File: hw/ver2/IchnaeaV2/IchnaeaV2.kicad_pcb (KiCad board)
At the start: 4 copper layers, 100 x 100 mm, 187 parts, among them J1 Screw_Terminal_01x09, J2 Screw_Terminal_01x09, J3 Screw_Terminal_01x09, Q1 BSS138, Q10 MCAC80N10Y, Q11 MCAC80N10Y, Q12 MCAC80N10Y, Q13 MCAC80N10Y, Q14 MCAC80N10Y, Q15 MCAC80N10Y, Q16 MCAC80N10Y, Q17 MCAC80N10Y, Q18 MCAC80N10Y, Q19 MCAC80N10Y, Q2 MCAC80N10Y, Q20 MCAC80N10Y, Q21 MCAC80N10Y, Q22 MCAC80N10Y, Q23 MCAC80N10Y, Q24 MCAC80N10Y, Q25 MCAC80N10Y, Q26 BSS138, Q27 BSS84, Q28 BSS138, Q29 BSS138, Q3 MCAC80N10Y, Q4 MCAC80N10Y, Q5 MCAC80N10Y, Q6 MCAC80N10Y, Q7 MCAC80N10Y, Q8 MCAC80N10Y, Q9 MCAC80N10Y, U1 LTC7871, U2 HIP2210, U3 HIP2210, U4 HIP2210, U5 HIP2210, U6 HIP2210, U7 HIP2210

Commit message: Sync work to main PC
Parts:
- removed D2, D3, D4, D5, D6, D7: Z5V1, Diode_SMD:D_SOD-123
- removed JP1, JP2: SolderJumper_2_Bridged, Jumper:SolderJumper-2_P1.3mm_Bridged_Pad1.0x1.5mm
- added C74: 10uF, Capacitor_SMD:C_0603_1608Metric, F.Cu at (162.4, 39.7)
- added C75: 4.7uF, Capacitor_SMD:C_0603_1608Metric, F.Cu at (162.4, 42.2)
- added C76: 100nF, Capacitor_SMD:C_0603_1608Metric, F.Cu at (162.4, 44.7)
- added C77: 47pF, Capacitor_SMD:C_0603_1608Metric, F.Cu at (162.4, 47.2)
- added C78: 10uF, Capacitor_SMD:C_0603_1608Metric, F.Cu at (166.4, 39.7)
- added C79: 10uF, Capacitor_SMD:C_0603_1608Metric, F.Cu at (166.4, 42.2)
- added C80: 10uF, Capacitor_SMD:C_0603_1608Metric, F.Cu at (166.4, 44.7)
- added C81: 10uF, Capacitor_SMD:C_0603_1608Metric, F.Cu at (166.4, 47.2)
- added C82: 10uF-100v, Capacitor_SMD:C_1210_3225Metric_Pad1.33x2.70mm_HandSolder, B.Cu at (168.1, 102.7)
- added C83: 10uF-100v, Capacitor_SMD:C_1210_3225Metric_Pad1.33x2.70mm_HandSolder, B.Cu at (171.4, 102.7)
- added D10: PMEG10010ELRX, Diode_SMD:D_SOD-123, F.Cu at (175.3, 40.1)
- added L7: 22uH, Inductors:TYS5020220M, F.Cu at (169.7, 51.5)
- added R54: 0, Resistor_SMD:R_0603_1608Metric, F.Cu at (126.7, 120.0)
- added R56: 0, Resistor_SMD:R_0603_1608Metric, F.Cu at (126.7, 121.2)
- added R57: 68k, Resistor_SMD:R_0603_1608Metric, F.Cu at (170.4, 39.7)
- added R58: 510k, Resistor_SMD:R_0603_1608Metric, F.Cu at (170.4, 42.2)
- added R59: 7.5k, Resistor_SMD:R_0603_1608Metric, F.Cu at (170.4, 44.7)
- added R60: 100k, Resistor_SMD:R_0603_1608Metric, F.Cu at (170.4, 47.2)
- added R61: 10k, Resistor_SMD:R_0603_1608Metric, F.Cu at (123.7, 117.6)
- added R62: 0, Resistor_SMD:R_0603_1608Metric, F.Cu at (126.7, 91.5)
- added R63: 0, Resistor_SMD:R_0603_1608Metric, F.Cu at (126.7, 90.0)
- added R64: 10k, Resistor_SMD:R_0603_1608Metric, F.Cu at (123.7, 87.9)
- added R65: 6.2k, Resistor_SMD:R_0603_1608Metric, F.Cu at (126.1, 87.2)
- added R66: 10k, Resistor_SMD:R_0603_1608Metric, F.Cu at (132.8, 84.2)
- added R67: 6.2k, Resistor_SMD:R_0603_1608Metric, F.Cu at (132.8, 87.2)
- added R68: 0, Resistor_SMD:R_0603_1608Metric, F.Cu at (160.1, 87.2)
- added R69: 10k, Resistor_SMD:R_0603_1608Metric, F.Cu at (162.3, 84.2)
- added R70: 6.2k, Resistor_SMD:R_0603_1608Metric, F.Cu at (163.8, 84.2)
- added R71: 0, Resistor_SMD:R_0603_1608Metric, F.Cu at (163.2, 90.9)
- added R72: 10k, Resistor_SMD:R_0603_1608Metric, F.Cu at (166.2, 93.1)
- added R73: 6.2k, Resistor_SMD:R_0603_1608Metric, F.Cu at (163.2, 93.1)
- added R74: 0, Resistor_SMD:R_0603_1608Metric, F.Cu at (163.3, 120.1)
- added R75: 10k, Resistor_SMD:R_0603_1608Metric, F.Cu at (166.3, 122.4)
- added R76: 6.2k, Resistor_SMD:R_0603_1608Metric, F.Cu at (163.3, 122.4)
- added U8: AP66200FVBW-13, Package_DFN_QFN:QFN-16-1EP_4x4mm_P0.65mm_EP2.5x2.5mm, F.Cu at (163.5, 51.6)
- C13, C19, C25, C31: value 100nF -> 10uF-100v; footprint Capacitor_SMD:C_0603_1608Metric -> Capacitor_SMD:C_1210_3225Metric_Pad1.33x2.70mm_HandSolder; moved to B.Cu
- D1: value SS210 -> SB10100L; footprint Diode_SMD:D_SMA -> Package_TO_SOT_SMD:TO-277A
- R12, R16, R20, R4, R8: value 2k -> 0
- R24: value 2k -> 6.2k
- moved J3 85.9 mm to (140.6, 144.0)
- moved C1 69.8 mm to (76.1, 134.1)
- moved C2 69.8 mm to (76.1, 136.6)
- moved R1 69.8 mm to (76.1, 144.1)
- moved R2 69.8 mm to (76.1, 146.6)
- moved R3 69.8 mm to (76.1, 149.1)
- moved R46 69.8 mm to (70.9, 143.0)
- moved R49 69.8 mm to (67.2, 145.2)
- moved R50 69.8 mm to (67.2, 147.7)
- moved C5 69.8 mm to (77.1, 156.0)
- moved D1 69.8 mm to (70.1, 156.1)
- moved Q1 69.8 mm to (82.6, 156.2)
- moved Q28 69.8 mm to (69.8, 139.7)
- moved Q29 69.8 mm to (72.0, 147.6)
- moved R51 69.8 mm to (69.5, 147.7)
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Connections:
- C12 pad 1: +VSW -> +12V
- C13 pad 1: +VSW -> VHIGH
- C18 pad 1: +VSW -> +12V
- C19 pad 1: +VSW -> VHIGH
- C24 pad 1: +VSW -> +12V
- C25 pad 1: +VSW -> VHIGH
- C30 pad 1: +VSW -> +12V
- C31 pad 1: +VSW -> VHIGH
- C36 pad 1: +VSW -> +12V
- C6 pad 1: +VSW -> +12V
- D1 pad 1: Net-(D1-K) -> VLOW
- L1 pad 1: Net-(Q2-S) -> VLOW
- L1 pad 2: VLOW -> Net-(Q2-S)
- L2 pad 1: VLOW -> Net-(Q6-S)
- L2 pad 2: Net-(Q6-S) -> VLOW
- L3 pad 1: Net-(Q10-S) -> VLOW
- L3 pad 2: VLOW -> Net-(Q10-S)
- L4 pad 1: VLOW -> Net-(Q14-S)
- L4 pad 2: Net-(Q14-S) -> VLOW
- L5 pad 1: Net-(Q18-S) -> VLOW
- L5 pad 2: VLOW -> Net-(Q18-S)
- L6 pad 1: VLOW -> Net-(Q22-S)
- L6 pad 2: Net-(Q22-S) -> VLOW
- R12 pad 1: Net-(D4-K) -> Net-(U4-EN)
- R12 pad 2: +VSW -> /PowerStage/Phase1/PWMEN
- R16 pad 1: Net-(D5-K) -> Net-(U5-EN)
- R16 pad 2: +VSW -> /PowerStage/Phase1/PWMEN
- R20 pad 1: Net-(D6-K) -> Net-(U5-PWM)
- R20 pad 2: +VSW -> /PowerStage/Phase4/PWM
- R24 pad 2: +VSW -> GND
- R4 pad 1: Net-(D2-K) -> Net-(U2-EN)
- R4 pad 2: +VSW -> /PowerStage/Phase1/PWMEN
- R8 pad 1: Net-(D3-K) -> Net-(U3-EN)
- R8 pad 2: +VSW -> /PowerStage/Phase1/PWMEN
- U2 pad 1: +VSW -> +12V
- U2 pad 5: Net-(D2-K) -> Net-(U2-VREF)
- U2 pad 7: /PowerStage/Phase1/PWMEN -> Net-(U2-EN)
- U3 pad 1: +VSW -> +12V
- U3 pad 5: Net-(D3-K) -> Net-(U3-VREF)
- U3 pad 7: /PowerStage/Phase1/PWMEN -> Net-(U3-EN)
- U3 pad 8: /PowerStage/Phase2/PWM -> Net-(U3-PWM)
- U4 pad 1: +VSW -> +12V
- U4 pad 5: Net-(D4-K) -> Net-(U4-VREF)
- U4 pad 7: /PowerStage/Phase1/PWMEN -> Net-(U4-EN)
- U4 pad 8: /PowerStage/Phase3/PWM -> Net-(U4-PWM)
- U5 pad 1: +VSW -> +12V
- U5 pad 5: Net-(D5-K) -> Net-(U5-VREF)
- U5 pad 7: /PowerStage/Phase1/PWMEN -> Net-(U5-EN)
- U5 pad 8: /PowerStage/Phase4/PWM -> Net-(U5-PWM)
- U6 pad 1: +VSW -> +12V
- U6 pad 5: Net-(D6-K) -> Net-(U6-VREF)
- U6 pad 7: /PowerStage/Phase1/PWMEN -> Net-(U6-EN)
- U6 pad 8: /PowerStage/Phase5/PWM -> Net-(U6-PWM)
- U7 pad 1: +VSW -> +12V
- U7 pad 7: /PowerStage/Phase1/PWMEN -> Net-(U7-EN)
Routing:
- net +12V: track 0.00 -> 54.6 mm, vias 0 -> 14
- net GND: track 2.74 -> 43.4 mm, vias 18 -> 49
- net Net-(Q14-G): track 0.00 -> 18.1 mm
- net Net-(Q22-G): track 0.00 -> 18.0 mm
- net Net-(Q6-G): track 0.00 -> 17.9 mm
- net Net-(Q23-G): track 0.00 -> 17.2 mm
- net Net-(Q15-G): track 0.00 -> 17.0 mm
- net Net-(Q7-G): track 0.00 -> 16.9 mm
- net Net-(Q3-G): track 0.00 -> 15.1 mm
- net Net-(Q11-G): track 0.00 -> 14.9 mm
- net Net-(U3-VREF): track 0.00 -> 14.8 mm
- net Net-(Q19-G): track 0.00 -> 14.8 mm
- net Net-(U5-VREF): track 0.00 -> 14.6 mm
- net Net-(U7-VREF): track 0.00 -> 14.1 mm
- net Net-(Q2-G): track 0.00 -> 13.5 mm
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- added copper zone on In2.Cu, net +12V
- added copper zone on F.Cu, net Net-(Q10-S)
- added copper zone on F.Cu, net Net-(Q14-S)
- added copper zone on F.Cu, net Net-(Q18-S)
- added copper zone on F.Cu, net Net-(Q2-S)
- added copper zone on F.Cu, net Net-(Q6-S)
- removed copper zone on F.Cu, net VHIGH
- removed copper zone on B.Cu, net VLOW

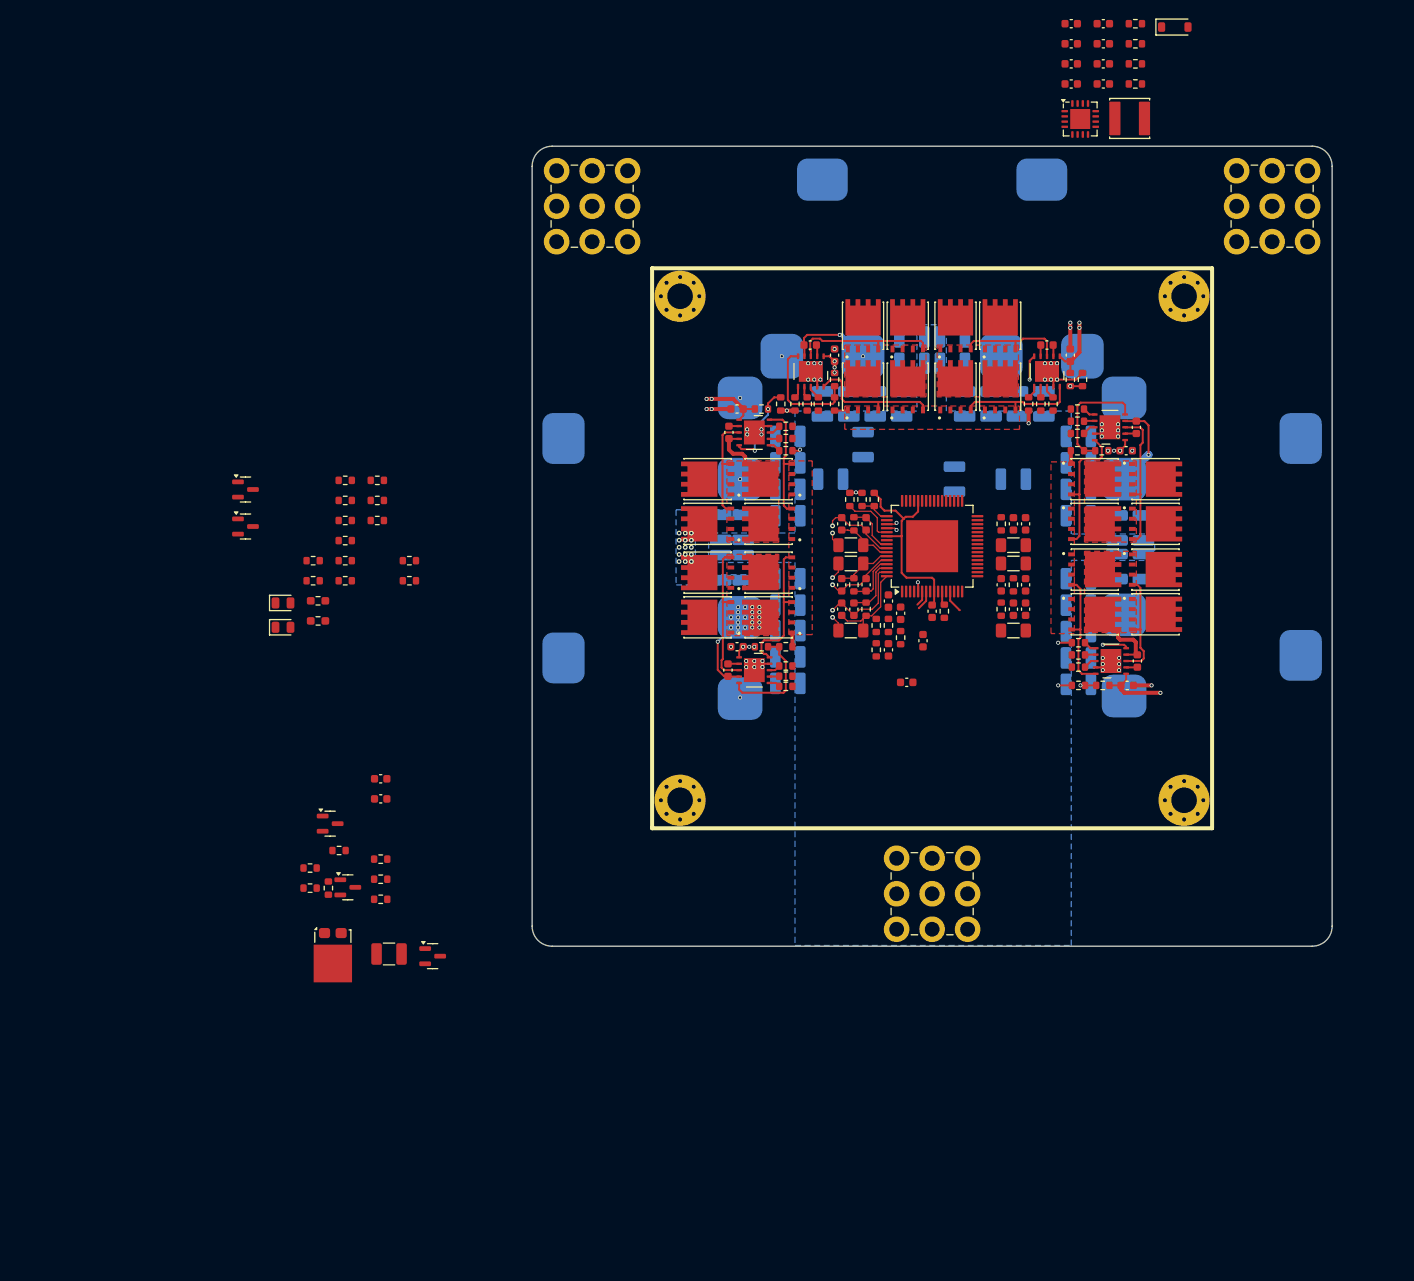
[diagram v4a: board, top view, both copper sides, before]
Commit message: More power stage layout
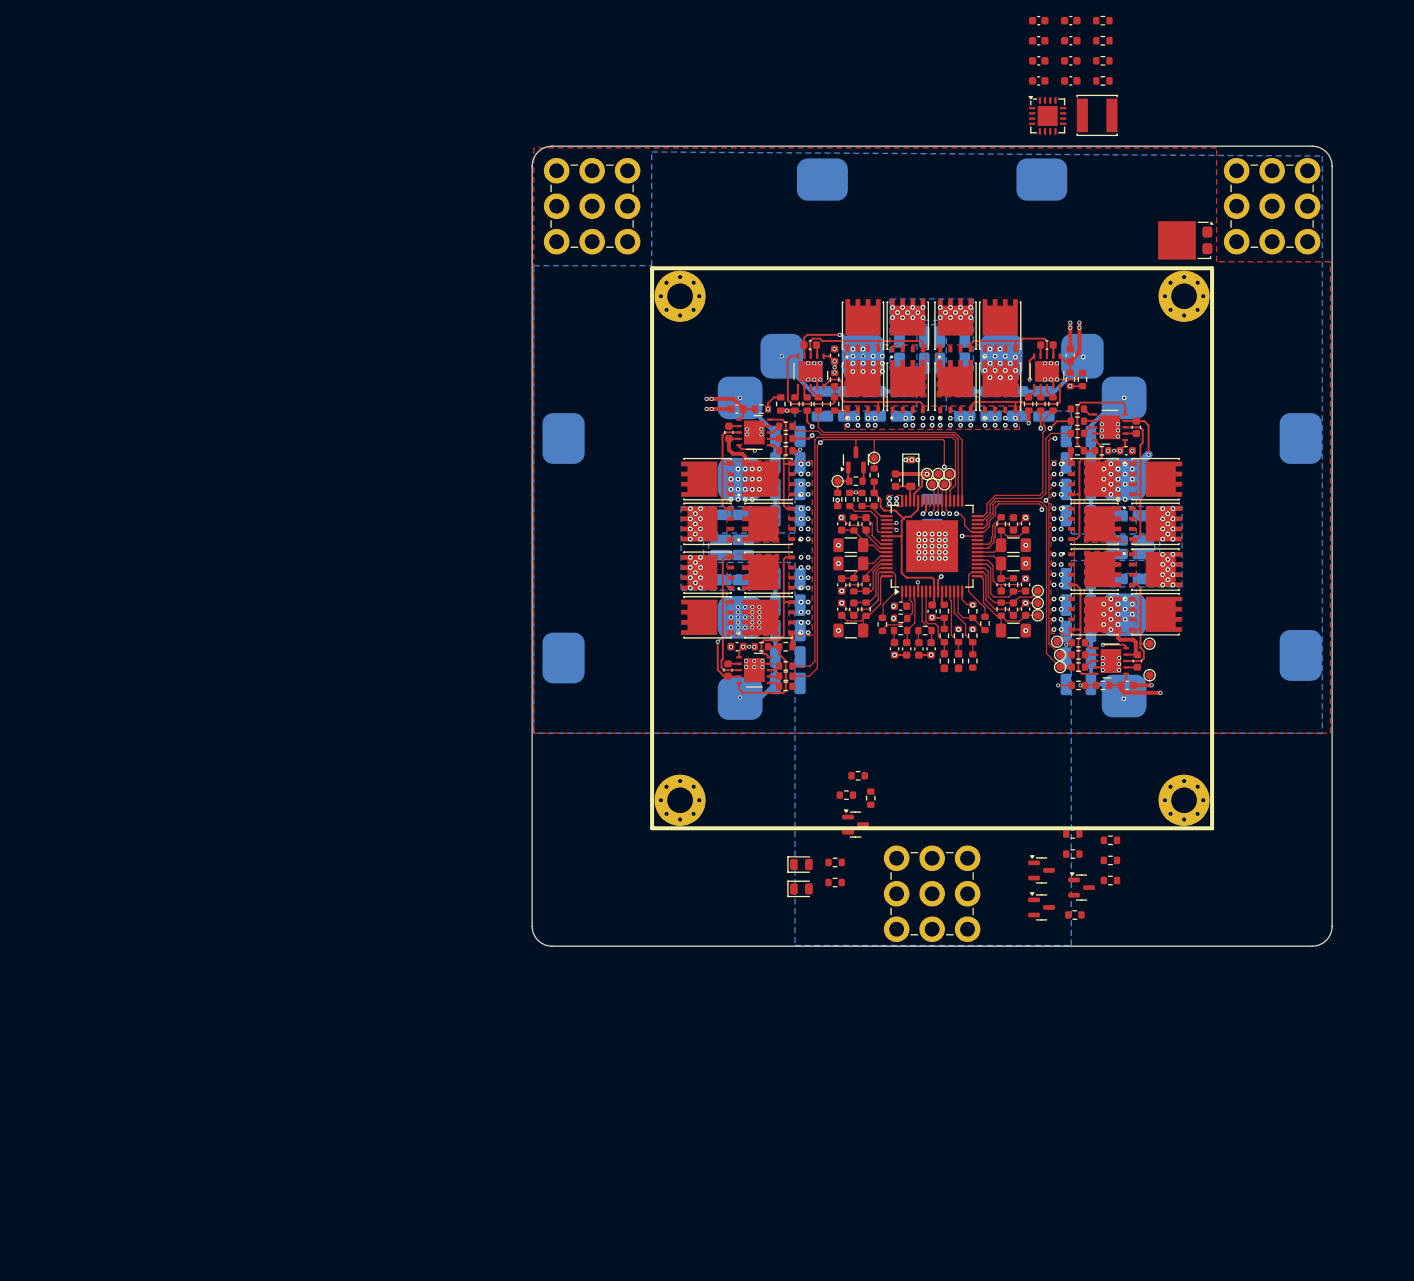
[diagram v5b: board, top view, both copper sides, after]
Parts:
- removed C2: 100nF, Capacitor_SMD:C_0603_1608Metric
- removed C23, C29, C49, C52: 10uF-100v, Capacitor_SMD:C_1210_3225Metric_Pad1.33x2.70mm_HandSolder
- removed D8, D9: Yellow LED, LED_SMD:LED_0805_2012Metric
- added D2: Yellow LED, LED_SMD:LED_0805_2012Metric, F.Cu at (128.7, 144.8)
- added D3: Yellow LED, LED_SMD:LED_0805_2012Metric, F.Cu at (128.7, 147.8)
- added TP1: TestPoint, TestPoint:TestPoint_Pad_D1.0mm, F.Cu at (145.0, 97.3)
- added TP10: TestPoint, TestPoint:TestPoint_Pad_D1.0mm, F.Cu at (172.2, 121.1)
- added TP11: TestPoint, TestPoint:TestPoint_Pad_D1.0mm, F.Cu at (158.2, 112.1)
- added TP12: TestPoint, TestPoint:TestPoint_Pad_D1.0mm, F.Cu at (158.2, 110.6)
- added TP13: TestPoint, TestPoint:TestPoint_Pad_D1.0mm, F.Cu at (158.2, 113.6)
- added TP14: TestPoint, TestPoint:TestPoint_Pad_D1.0mm, F.Cu at (133.2, 96.9)
- added TP15: TestPoint, TestPoint:TestPoint_Pad_D1.0mm, F.Cu at (137.8, 94.0)
- added TP2: TestPoint, TestPoint:TestPoint_Pad_D1.0mm, F.Cu at (145.8, 96.0)
- added TP3: TestPoint, TestPoint:TestPoint_Pad_D1.0mm, F.Cu at (146.5, 97.3)
- added TP4: TestPoint, TestPoint:TestPoint_Pad_D1.0mm, F.Cu at (147.2, 96.0)
- added TP5: TestPoint, TestPoint:TestPoint_Pad_D1.0mm, F.Cu at (144.4, 96.0)
- added TP6: TestPoint, TestPoint:TestPoint_Pad_D1.0mm, F.Cu at (161.0, 118.6)
- added TP7: TestPoint, TestPoint:TestPoint_Pad_D1.0mm, F.Cu at (161.0, 120.1)
- added TP8: TestPoint, TestPoint:TestPoint_Pad_D1.0mm, F.Cu at (160.6, 116.9)
- added TP9: TestPoint, TestPoint:TestPoint_Pad_D1.0mm, F.Cu at (172.2, 117.2)
- C5: moved to B.Cu
- moved D1 139.1 mm to (176.6, 66.8), turned to -90 degrees
- moved Q26 110.3 mm to (158.7, 145.5)
- moved Q27 110.3 mm to (158.7, 150.2)
- moved R43 102.1 mm to (167.3, 141.8)
- moved R44 102.1 mm to (167.3, 144.3)
- moved R45 102.1 mm to (167.3, 146.8)
- moved R41 97.2 mm to (162.6, 141.0)
- moved R42 97.2 mm to (162.6, 143.5)
- moved Q28 94.3 mm to (163.7, 147.7)
- moved R46 92.3 mm to (162.8, 151.1)
- moved C5 87.6 mm to (145.0, 100.7), turned to -90 degrees
- moved R35 84.1 mm to (151.6, 114.7), turned to -90 degrees
- moved R34 83.4 mm to (150.1, 119.4), turned to 90 degrees
- moved Q1 81.5 mm to (135.5, 94.2), turned to 90 degrees
- moved R33 80.4 mm to (148.3, 119.4), turned to 90 degrees
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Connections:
- R3 pad 2: unconnected-(R3-Pad2) -> /PowerStage/IO_LTC_PWM_EN
- U1 pad 30: PGOOD -> unconnected-(U1-PGOOD-Pad30)
- U1 pad 35: FAULT -> unconnected-(U1-FAULT-Pad35)
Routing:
- net VLOW: track 109.2 -> 336.3 mm, vias 6 -> 12
- net /PowerStage/Phase1/PWMEN: track 0.00 -> 124.5 mm, vias 0 -> 10
- net /PowerStage/Phase6/PWM: track 0.00 -> 56.5 mm
- net /PowerStage/IO_LTC_PWM_EN: track 0.00 -> 34.2 mm, vias 0 -> 1
- net /PowerStage/Phase1/PWM: track 0.00 -> 33.5 mm
- net /PowerStage/IO_LTC_SDI: track 0.00 -> 33.4 mm, vias 0 -> 1
- net /PowerStage/IO_LTC_SCK: track 0.00 -> 32.8 mm, vias 0 -> 1
- net /PowerStage/IO_LTC_CSB: track 0.00 -> 32.7 mm, vias 0 -> 1
- net /PowerStage/IO_LTC_SDO: track 0.00 -> 31.8 mm, vias 0 -> 1
- net Net-(Q6-S): track 11.2 -> 42.1 mm, vias 1 -> 19
- net /PowerStage/Phase5/PWM: track 0.00 -> 29.1 mm
- net /PowerStage/Phase4/PWM: track 0.00 -> 28.3 mm
- net LTC_MODE: track 1.29 -> 29.1 mm
- net LTC_RUN: track 0.00 -> 27.5 mm, vias 0 -> 1
- net LTC_SYNC: track 1.31 -> 27.2 mm
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- added copper zone on In1.Cu, net Net-(D1-K)
- added copper zone on F.Cu, net VHIGH
- added copper zone on In1.Cu, net VHIGH
- added copper zone on B.Cu, net VLOW

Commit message: Sync
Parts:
- removed C74: 10uF, Capacitor_SMD:C_0603_1608Metric
- added C2: 10uF-100v, Capacitor_SMD:C_1210_3225Metric_Pad1.33x2.70mm_HandSolder, F.Cu at (185.3, 78.5)
- moved C75 56.5 mm to (188.7, 89.5), turned to -90 degrees
- moved R57 54.3 mm to (183.4, 90.9)
- moved R58 53.4 mm to (183.4, 92.4)
- moved C78 51.4 mm to (188.7, 83.4), turned to 90 degrees
- moved C77 50.9 mm to (190.2, 86.5), turned to 90 degrees
- moved C79 50.1 mm to (190.2, 83.4), turned to 90 degrees
- moved C80 48.9 mm to (191.7, 83.4), turned to 90 degrees
- moved C76 48.8 mm to (182.0, 87.0), turned to -90 degrees
- moved C81 47.9 mm to (193.3, 83.4), turned to 90 degrees
- moved R59 47.7 mm to (188.7, 86.5), turned to 90 degrees
- moved R60 47.1 mm to (191.7, 86.5), turned to 90 degrees
- moved U8 44.9 mm to (185.3, 87.9), turned to -90 degrees
- moved L7 37.1 mm to (185.3, 82.6), turned to 180 degrees
- moved D1 10.7 mm to (185.3, 73.1), turned to 0 degrees
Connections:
- U8 pad 1: /PowerStage/VOUT_LV -> +12V
